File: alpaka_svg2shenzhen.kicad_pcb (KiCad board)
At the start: 2 copper layers, 39.6 x 49.3 mm, 10 parts, among them SW1 SW_DPDT_x2

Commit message: updated back silk text
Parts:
- removed the G*** at (90.0, 48.9) (x5)
- removed the G*** at (0.00, 0.00) (x2)
- added G*** (x5): LOGO, LOGO, F.Cu at (90.0, 48.9)
- added G*** (x2): LOGO, LOGO, F.Cu at (0.00, 0.00)
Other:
- board text added: "Alex Kutschera 11-09-2021"
- board text added: "oberlab.de"

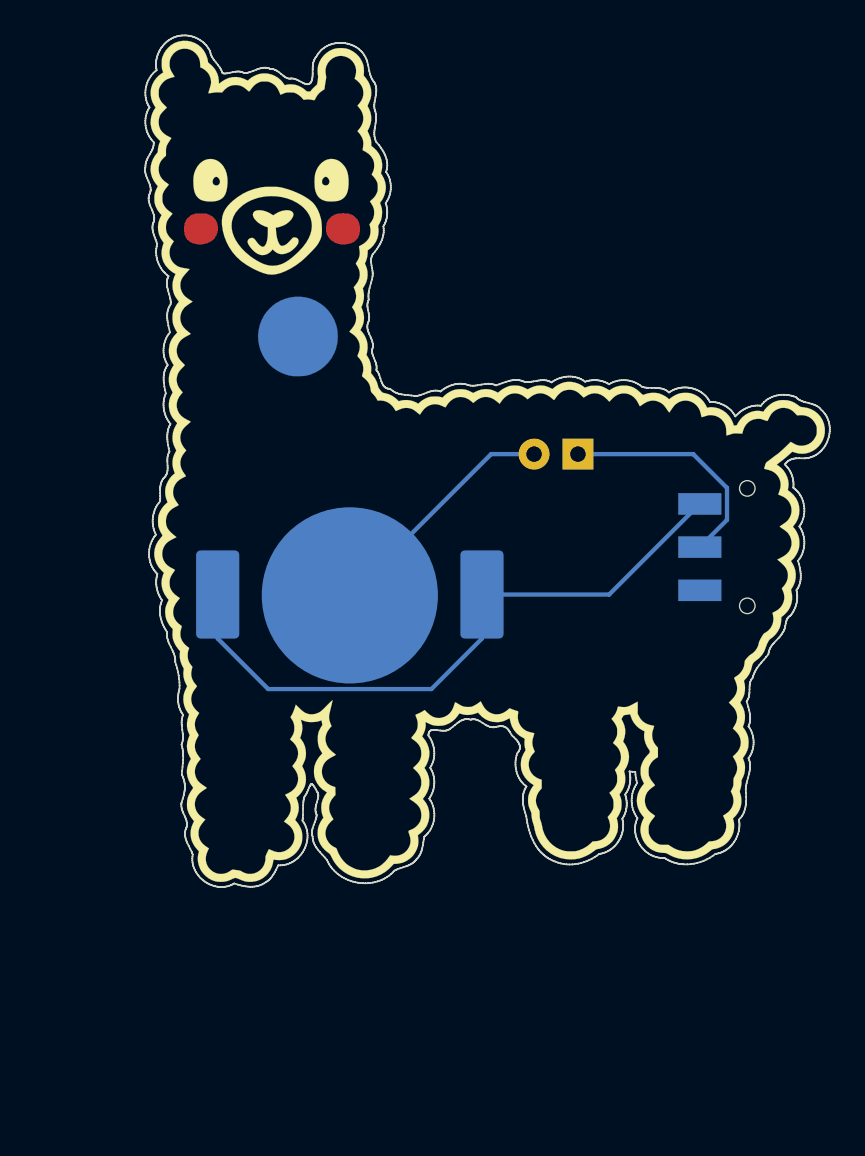
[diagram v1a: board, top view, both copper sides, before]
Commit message: fixed wrong connections, increased size of pin pad
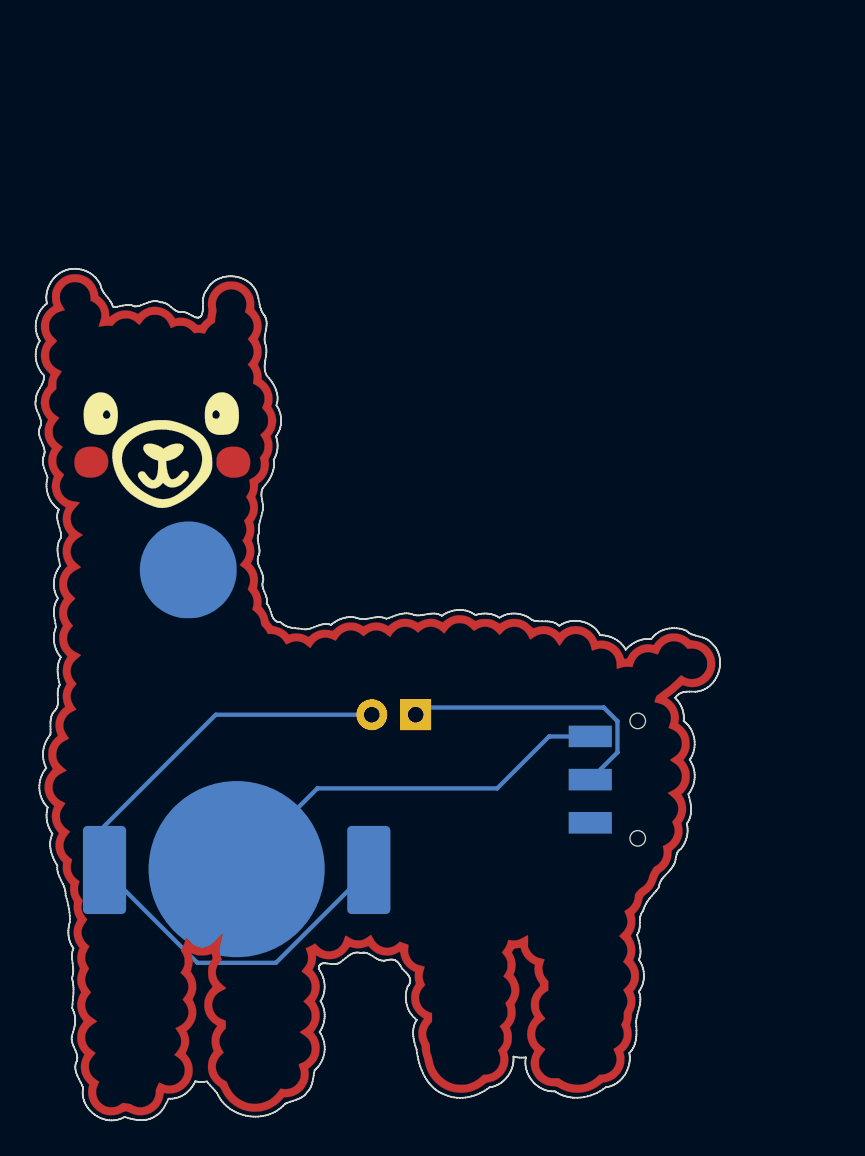
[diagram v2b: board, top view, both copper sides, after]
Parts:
- removed the G*** at (90.0, 48.9) (x5)
- removed the G*** at (0.00, 0.00) (x2)
- added G*** (x5): LOGO, LOGO, F.Cu at (83.6, 62.4)
- added G*** (x2): LOGO, LOGO, F.Cu at (0.00, 0.00)
- moved D1 17.8 mm to (85.8, 63.6)
- moved BT1 17.2 mm to (75.4, 72.5), turned to 0 degrees
- moved SW1 14.9 mm to (98.7, 67.3)
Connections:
- BT1 pad 1: Net-(BT1-Pad1) -> Net-(BT1-Pad2)
- BT1 pad 2: Net-(BT1-Pad2) -> Net-(BT1-Pad1)
- BT1 pad 3: Net-(BT1-Pad2) -> Net-(BT1-Pad1)
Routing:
- net Net-(BT1-Pad1): track 14.1 -> 40.4 mm
- net Net-(BT1-Pad2): track 37.6 -> 23.7 mm
- net Net-(D1-Pad1): track 13.5 -> 16.2 mm
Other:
- outline, holes or cut-outs redrawn
- board text added: "Alex Kutschera 12-09-2021"
- board text removed: "Alex Kutschera 11-09-2021"
